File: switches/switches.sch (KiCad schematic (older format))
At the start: 44 parts, among them J1 switchesOut, J10 Conn_01x01_Female, J11 Conn_01x01_Female, J12 Conn_01x01_Female, J2 Conn_01x01_Female, J3 Conn_01x01_Female, J4 Conn_01x01_Female, J5 Conn_01x01_Female, J6 Conn_01x01_Female, J7 Conn_01x01_Female, J8 Conn_01x01_Female, J9 Conn_01x01_Female, Q1 2N7002, Q2 2N7002, Q3 2N7002, Q4 2N7002, Q5 2N7002, Q6 2N7002

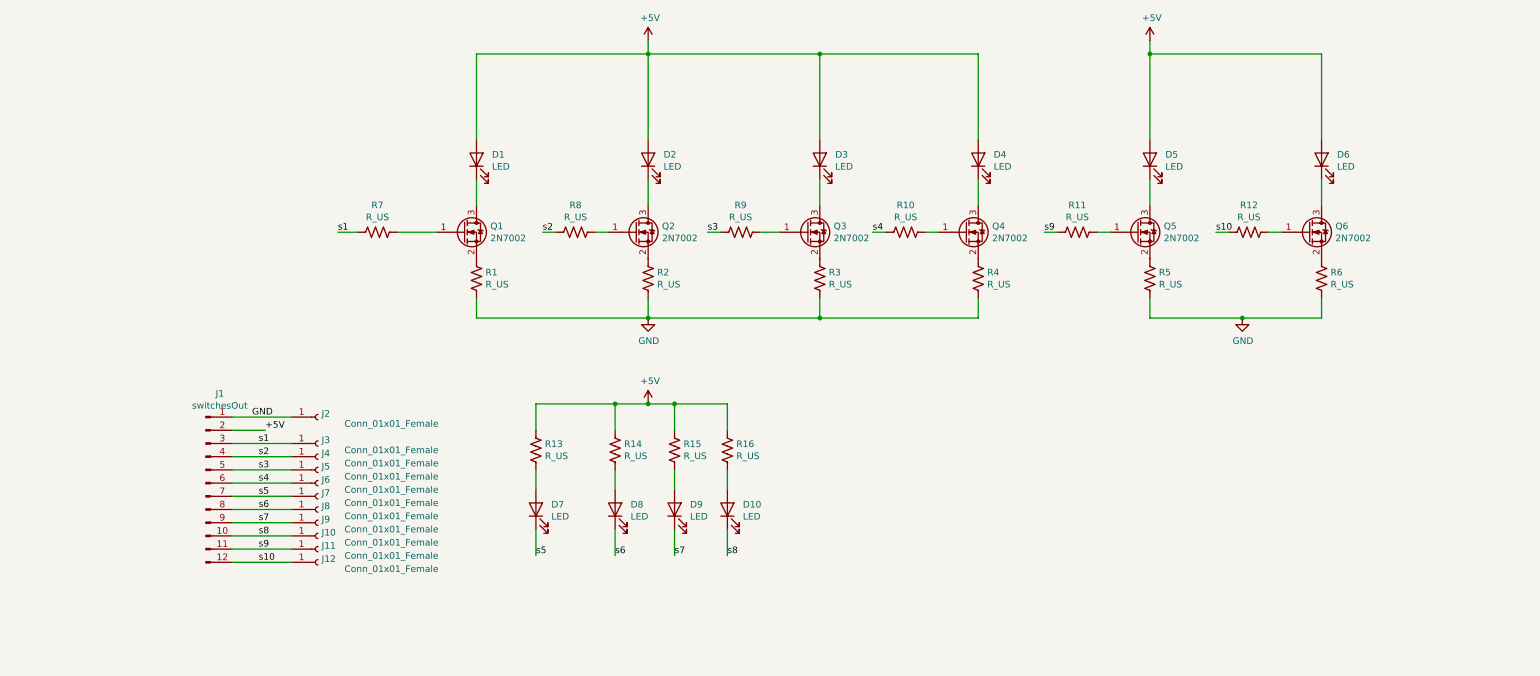
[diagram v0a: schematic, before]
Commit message: [vishnu] Added comments in the schematic for easy understanding. 	 Can also double as technical document.
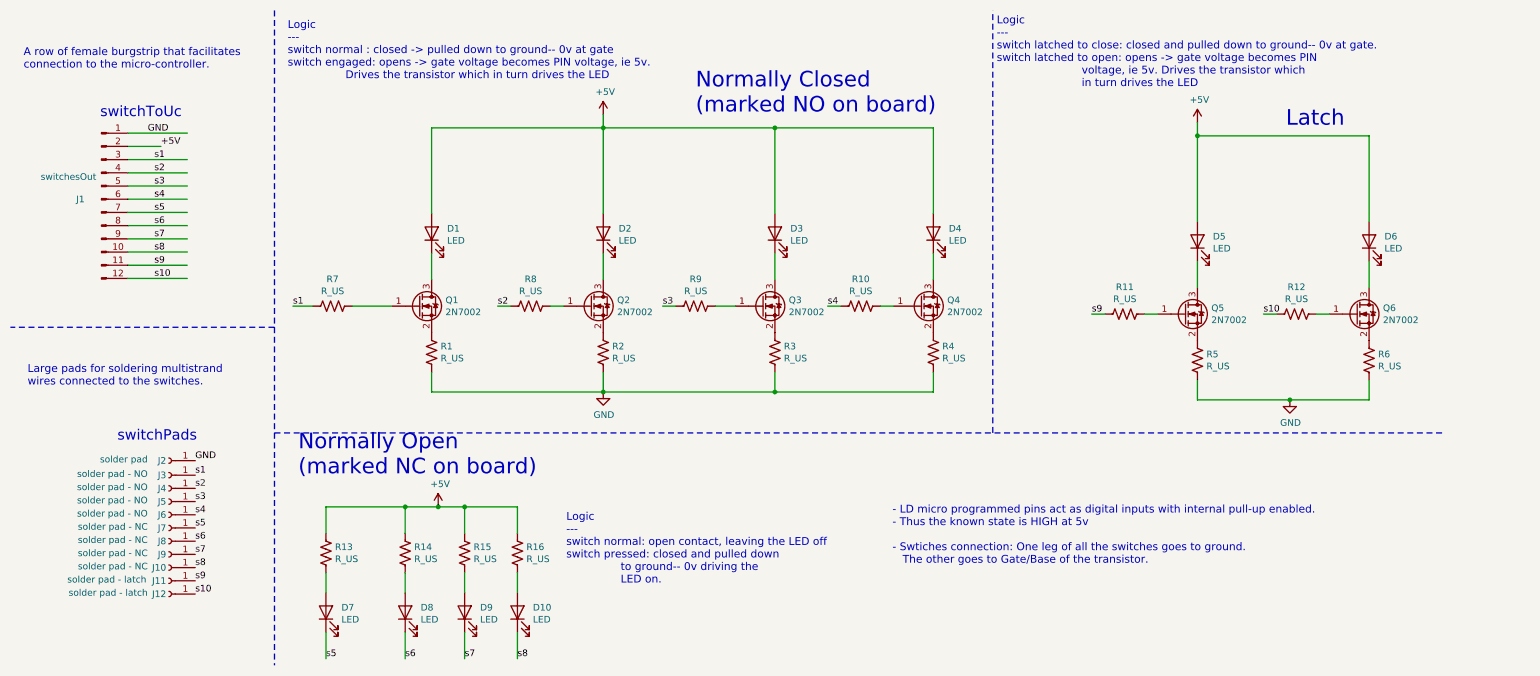
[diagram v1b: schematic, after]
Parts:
- J10, J7, J8, J9: value Conn_01x01_Female -> solder pad - NC
- J11, J12: value Conn_01x01_Female -> solder pad - latch
- J2: value Conn_01x01_Female -> solder pad
- J3, J4, J5, J6: value Conn_01x01_Female -> solder pad - NO
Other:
- note added: "- LD micro programmed pins act as digital inputs with internal pull-up enabled.\n- Thus the known state is HIGH at 5v\n\n- Swtiches connection: One leg of all the switches goes to ground. \n The other goes to Gate/Base of the transistor."
- note added: "A row of female burgstrip that facilitates \nconnection to the micro-controller."
- note added: "Large pads for soldering multistrand\nwires connected to the switches."
- note added: "Latch"
- note added: "Logic\n---\nswitch latched to close: closed and pulled down to ground-- 0v at gate.\nswitch latched to open: opens -> gate voltage becomes PIN \n voltage, ie 5v. Drives the transistor which \n in turn drives the LED\n"
- note added: "Logic\n---\nswitch normal : closed -> pulled down to ground-- 0v at gate\nswitch engaged: opens -> gate voltage becomes PIN voltage, ie 5v.\n Drives the transistor which in turn drives the LED\n"
- note added: "Logic\n---\nswitch normal: open contact, leaving the LED off\nswitch pressed: closed and pulled down \n to ground-- 0v driving the \n LED on.\n"
- note added: "Normally Closed \n(marked NO on board)"
- note added: "Normally Open\n(marked NC on board)"
- note added: "switchPads"
- note added: "switchToUc"
- moved on the sheet: D1, D10, D2, D3, D4, D5, D6, D7, D8, D9, J1, J10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
